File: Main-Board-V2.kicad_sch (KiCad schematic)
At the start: 5 parts, among them IC2 REG1117-5, J2 BCS-114-L-S-PE-BE, J3 BCS-114-L-S-PE-BE

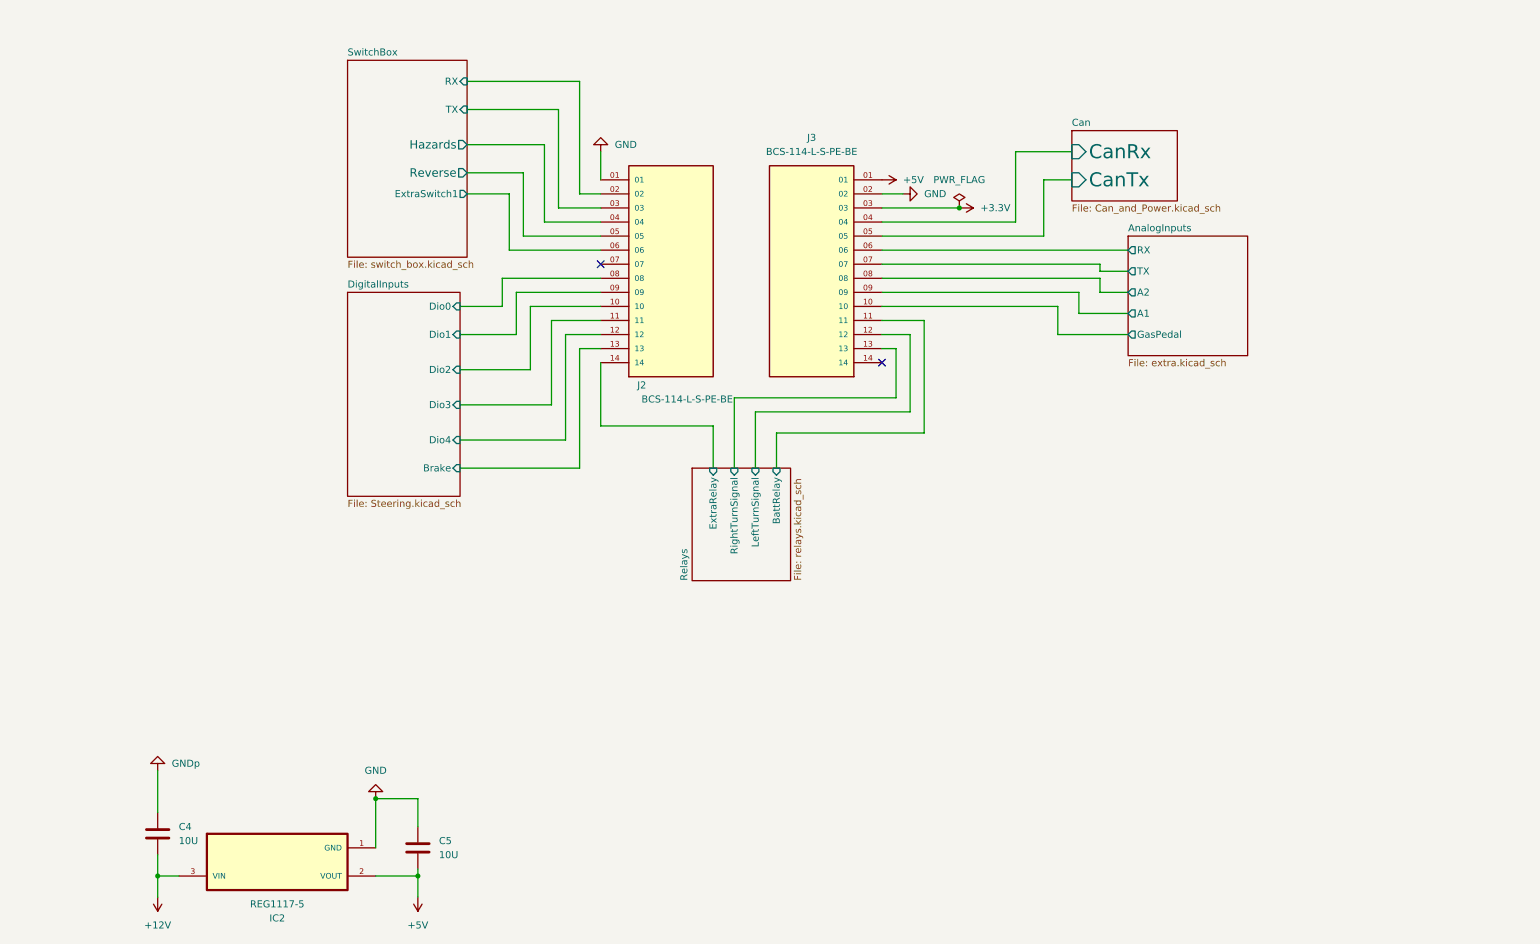
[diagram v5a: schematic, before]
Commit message: Moved everything to 23-POS AmpSeal
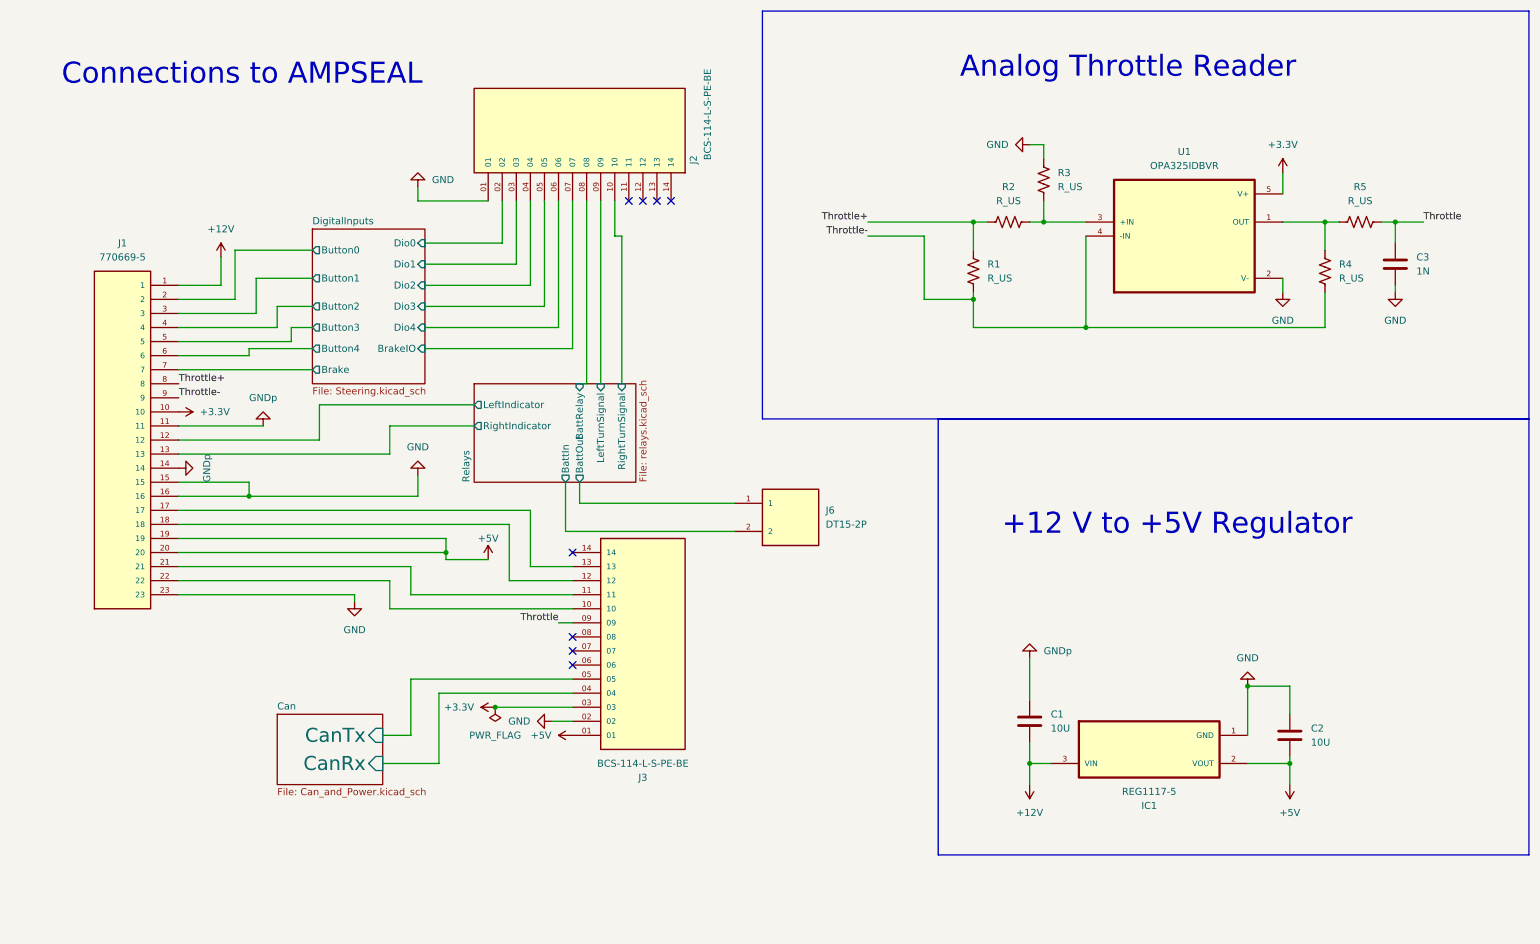
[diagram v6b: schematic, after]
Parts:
- added C3: 1N, symbol Device:C
- added J1: 770669-5, 770669-5:TE_770669-5, symbol 770669-5:770669-5
- added J6: DT15-2P, DT15-2P:TE_DT15-2P, symbol DT15-2P:DT15-2P
- added R1, R2, R3, R4, R5: R_US, symbol Device:R_US
- added U1: OPA325IDBVR, OPA325IDBVR:SOT95P280X145-5N, symbol OPA325IDBVR:OPA325IDBVR
- renumbered C4 to C1, C5 to C2, IC2 to IC1
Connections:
- net SwitchBox/ExtraSwitch1 is gone; now on net DigitalInputs/Dio4: J2.06
- net SwitchBox/Hazards is gone; now on net DigitalInputs/Dio2: J2.04
- net SwitchBox/RX is gone; now on net DigitalInputs/Dio0: J2.02
- net SwitchBox/Reverse is gone; now on net DigitalInputs/Dio3: J2.05
- net SwitchBox/TX is gone; now on net DigitalInputs/Dio1: J2.03
- net +12V: now also J1.1
- net +3.3V: now also J1.10, U1.5 (V+)
- net +5V: now also J1.19, J1.20
- net DigitalInputs/Brake: now also J1.7; no longer J2.13
- net DigitalInputs/Dio0: no longer J2.08
- net DigitalInputs/Dio1: no longer J2.09
- net DigitalInputs/Dio2: no longer J2.10
- net DigitalInputs/Dio3: no longer J2.11
- net DigitalInputs/Dio4: no longer J2.12
- net GND: now also C3.2, J1.15, J1.16, J1.23, R3.1, U1.2 (V-)
- net GNDp: now also J1.11, J1.14
- net Relays/BattRelay: now also J2.08; no longer J3.11
- net Relays/LeftTurnSignal: now also J2.09; no longer J3.12
- net Relays/RightTurnSignal: now also J2.10; no longer J3.13
- net DigitalInputs/BrakeIO: now reaches J2.07
- net AnalogInputs/A1 renamed Throttle
- net Throttle: now also C3.1, R5.2
- net AnalogInputs/A2: no longer names the net of J3.08
- net AnalogInputs/GasPedal: no longer names the net of J3.10
- net AnalogInputs/GasPedal: now also J1.22
- net AnalogInputs/RX: no longer names the net of J3.06
- net AnalogInputs/TX: no longer names the net of J3.07
- net Relays/ExtraRelay: no longer names the net of J2.14
- new net: R4.2, R5.1, U1.1 (OUT)
- new net: R2.2, R3.2, U1.3 (+IN)
- new net: J1.17, J3.13
- new net: J1.18, J3.12
- new net: J1.21, J3.11
- new net DigitalInputs/Button0: J1.2
- new net DigitalInputs/Button1: J1.3
- new net DigitalInputs/Button2: J1.4
- new net DigitalInputs/Button3: J1.5
- new net DigitalInputs/Button4: J1.6
- new net Relays/BattIn: J6.2
- new net Relays/BattOut: J6.1
- new net Relays/LeftIndicator: J1.12
- new net Relays/RightIndicator: J1.13
- new net Throttle+: J1.8, R1.1, R2.1
- new net Throttle-: J1.9, R1.2, R4.1, U1.4 (-IN)
- no-connect marks 2 -> 8
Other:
- removed sheet AnalogInputs
- removed sheet SwitchBox
- sheet DigitalInputs ports: added BrakeIO, Button0, Button1, Button2, Button3, Button4; removed none
- sheet Relays ports: added BattIn, BattOut, LeftIndicator, RightIndicator; removed ExtraRelay
- note added: "+12 V to +5V Regulator"
- note added: "Analog Throttle Reader"
- note added: "Connections to AMPSEAL"
- moved on the sheet: C1, C2, IC1, J2, J3

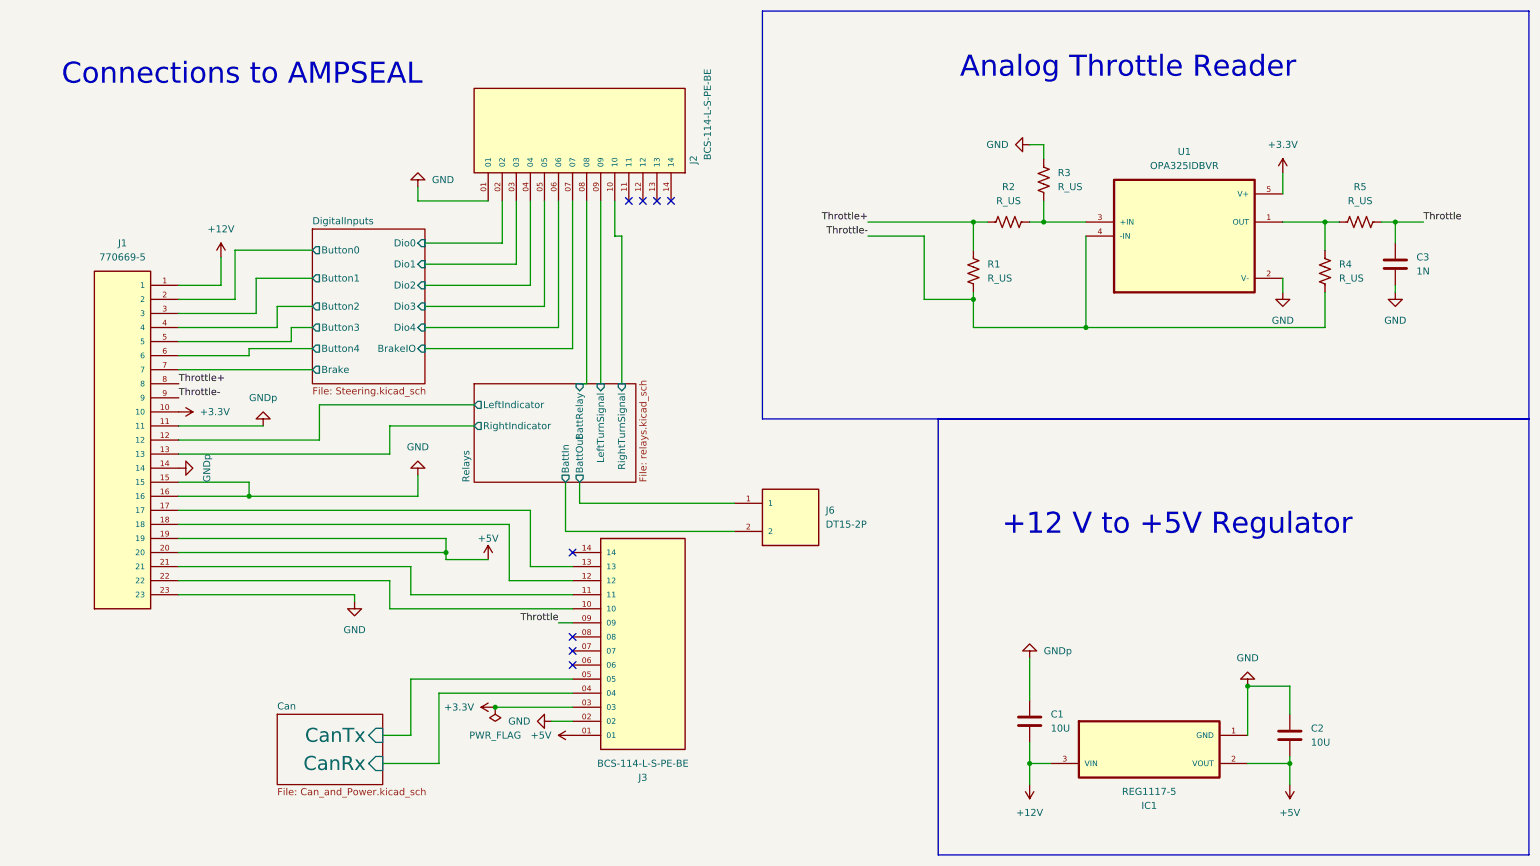
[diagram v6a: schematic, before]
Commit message: Final Pinout for connectors
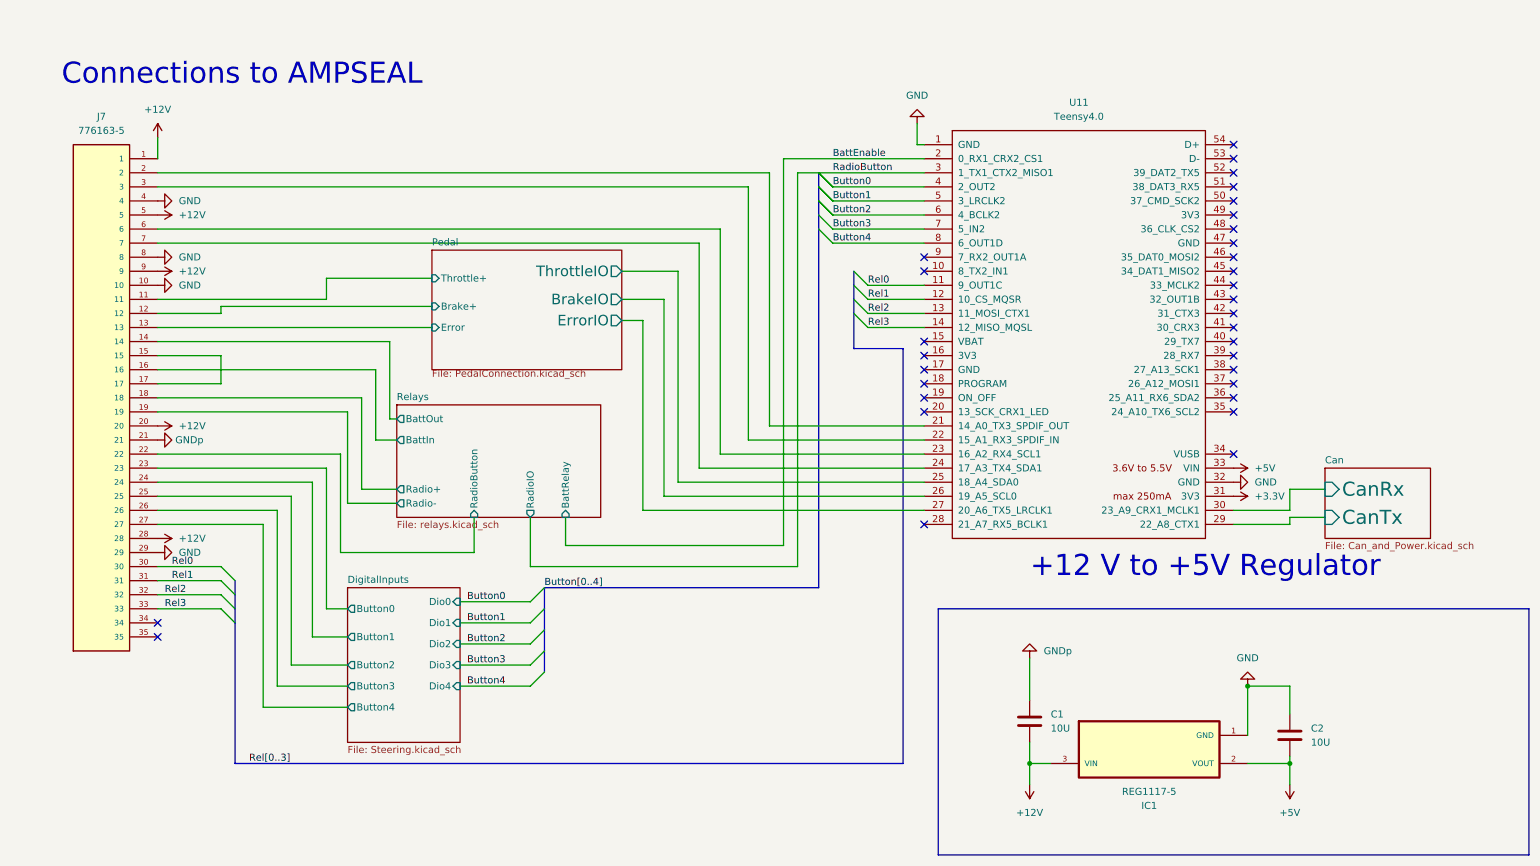
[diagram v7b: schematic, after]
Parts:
- removed C3: 1N, symbol Device:C
- removed J1: 770669-5, 770669-5:TE_770669-5, symbol 770669-5:770669-5
- removed J2, J3: BCS-114-L-S-PE-BE, BCS:SAMTEC_BCS-114-L-S-PE-BE, symbol BCS-114-L-S-PE-BE:BCS-114-L-S-PE-BE
- removed J6: DT15-2P, DT15-2P:TE_DT15-2P, symbol DT15-2P:DT15-2P
- removed R1, R2, R3, R4, R5: R_US, symbol Device:R_US
- removed U1: OPA325IDBVR, OPA325IDBVR:SOT95P280X145-5N, symbol OPA325IDBVR:OPA325IDBVR
- added J7: 776163-5, 776163-5:TE_776163-5, symbol 776163-5:776163-5
- added U11: Teensy4.0, symbol teensy:Teensy4.0
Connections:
- net +12V: now also J7.1, J7.20, J7.28, J7.5, J7.9
- net +3.3V: now also U11.31 (3V3)
- net +5V: now also U11.33 (VIN)
- net Can/CanRx: now also U11.30 (23_A9_CRX1_MCLK1)
- net Can/CanTx: now also U11.29 (22_A8_CTX1)
- net DigitalInputs/Button0: now also J7.23
- net DigitalInputs/Button1: now also J7.24
- net DigitalInputs/Button2: now also J7.25
- net DigitalInputs/Button3: now also J7.26
- net DigitalInputs/Button4: now also J7.27
- net GND: now also J7.10, J7.29, J7.4, J7.8, U11.1 (GND), U11.32 (GND)
- net GNDp: now also J7.21
- net Relays/BattIn: now also J7.16
- net Relays/BattOut: now also J7.14
- new net: J7.15, J7.17
- new net: J7.2, U11.21 (14_A0_TX3_SPDIF_OUT)
- new net: J7.3, U11.22 (15_A1_RX3_SPDIF_IN)
- new net: J7.6, U11.23 (16_A2_RX4_SCL1)
- new net: J7.7, U11.24 (17_A3_TX4_SDA1)
- new net BattEnable: U11.2 (0_RX1_CRX2_CS1)
- new net Button0: U11.4 (2_OUT2)
- new net Button1: U11.5 (3_LRCLK2)
- new net Button2: U11.6 (4_BCLK2)
- new net Button3: U11.7 (5_IN2)
- new net Button4: U11.8 (6_OUT1D)
- new net Pedal/Brake+: J7.12
- new net Pedal/BrakeIO: U11.26 (19_A5_SCL0)
- new net Pedal/Error: J7.13
- new net Pedal/ErrorIO: U11.27 (20_A6_TX5_LRCLK1)
- new net Pedal/Throttle+: J7.11
- new net Pedal/ThrottleIO: U11.25 (18_A4_SDA0)
- new net RadioButton: U11.3 (1_TX1_CTX2_MISO1)
- new net Rel0: J7.30, U11.11 (9_OUT1C)
- new net Rel1: J7.31, U11.12 (10_CS_MQSR)
- new net Rel2: J7.32, U11.13 (11_MOSI_CTX1)
- new net Rel3: J7.33, U11.14 (12_MISO_MQSL)
- new net Relays/Radio+: J7.18
- new net Relays/Radio-: J7.19
- new net Relays/RadioButton: J7.22
- no-connect marks 8 -> 32
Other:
- added sheet Pedal (PedalConnection.kicad_sch)
- sheet DigitalInputs ports: added none; removed Brake, BrakeIO
- sheet Relays ports: added Radio+, Radio-, RadioButton, RadioIO; removed LeftIndicator, LeftTurnSignal, RightIndicator, RightTurnSignal
- note removed: "Analog Throttle Reader"

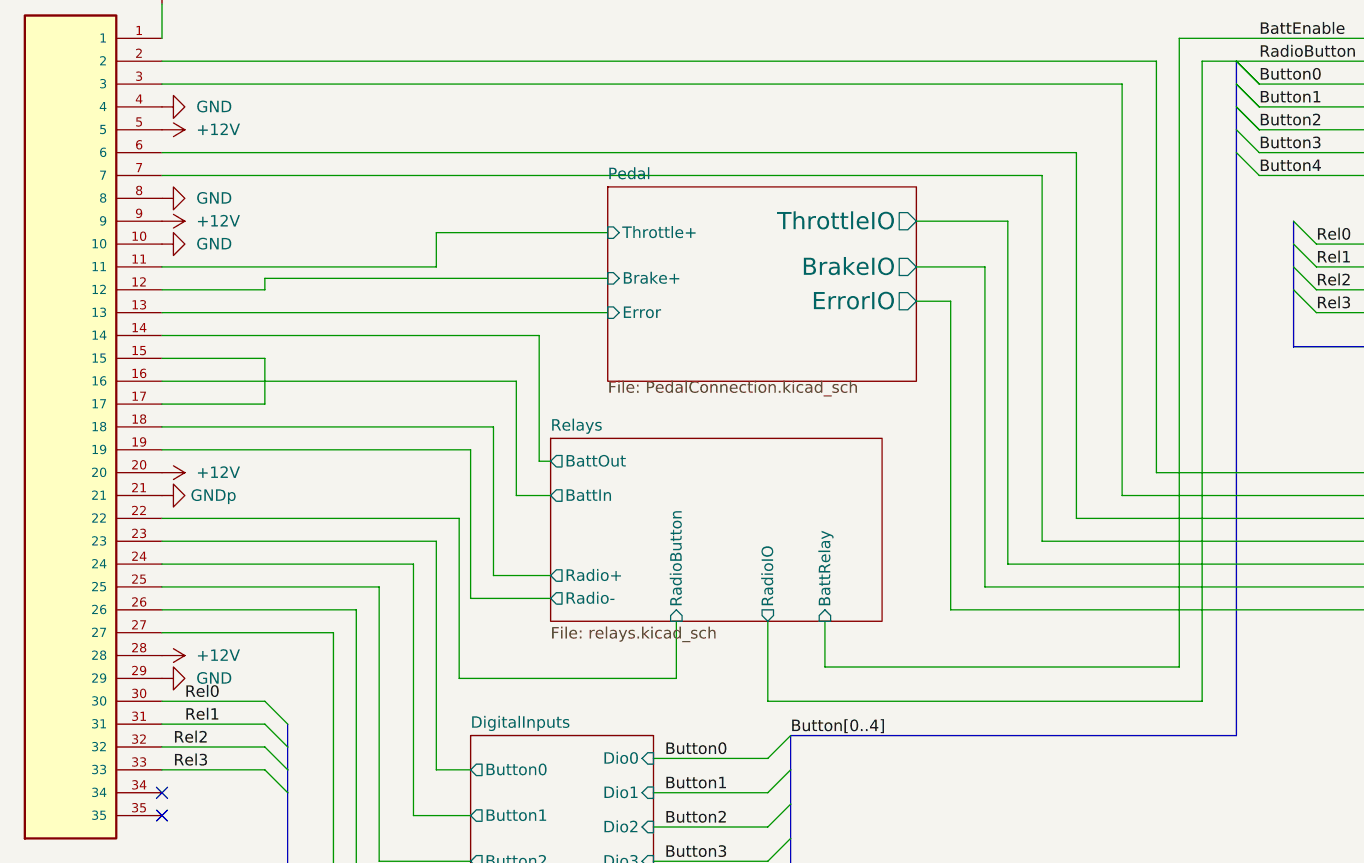
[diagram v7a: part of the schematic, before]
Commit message: Swapped battery relay pins
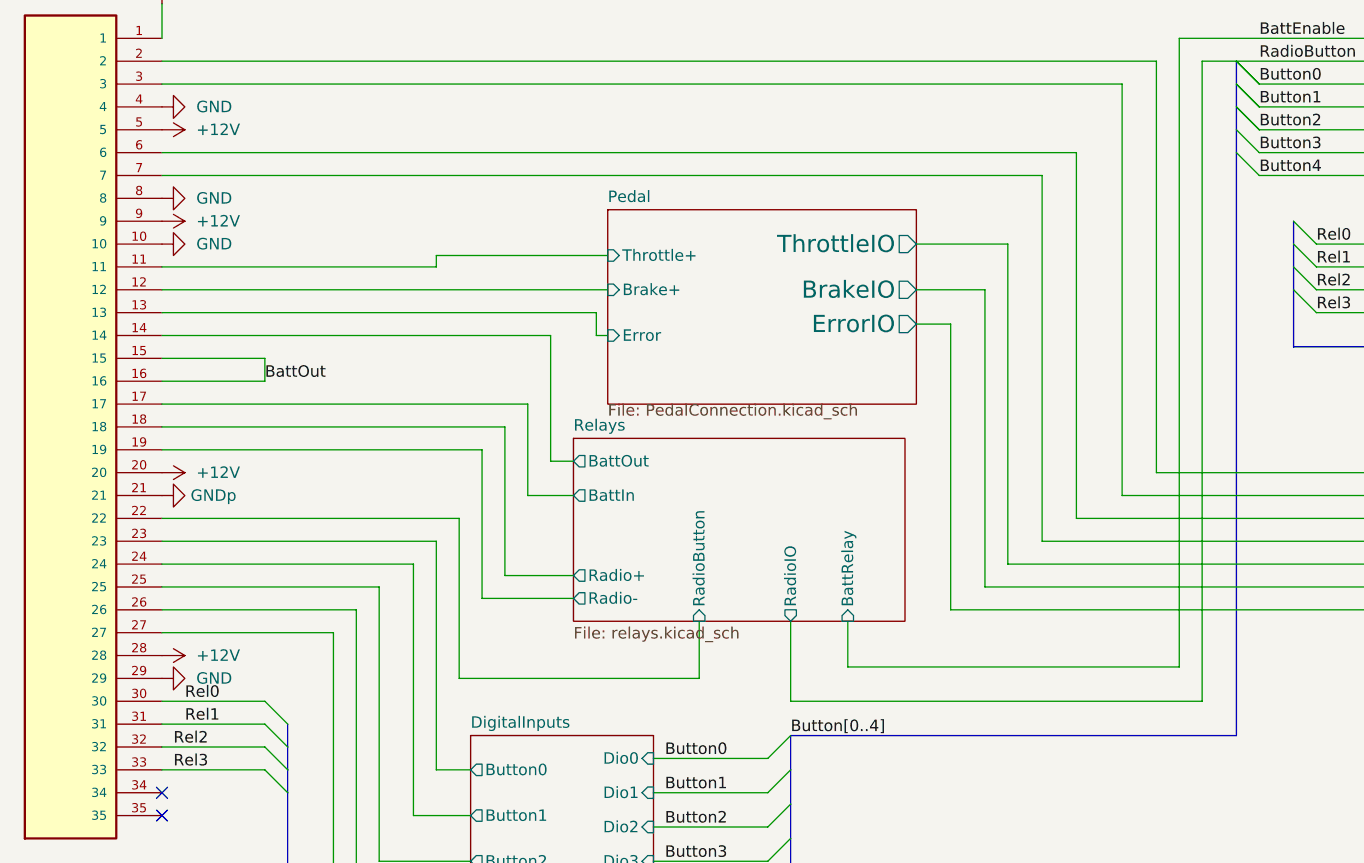
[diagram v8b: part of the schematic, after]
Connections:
- net Relays/BattIn: now also J7.17; no longer J7.16
- net BattOut: now reaches J7.15
- net BattOut: now also J7.16; no longer J7.17
